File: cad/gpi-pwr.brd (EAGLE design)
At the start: 130 x 73.5 mm, 104 parts, among them CN1 HEADER-1X2, CN2 HEADER-3X1, CN3 HEADER-1X2.4, CN4 HEADER-3X12MM, Q1 MOSFETTO247REV, Q3 MOSFETTO247REV, Q5 MOSFETTO247REV, Q6 MOSFETTO247REV, Q7 MOSFETTO247REV, Q8 MOSFETTO247REV, U1 ACS709, U10 LM61, U11 MAX4452, U12 MAX4452, U2 ACS709, U3 ACPL-P346P346, U4 ACPL-P346P346, U5 ACPL-P346P346, U6 ACPL-P346P346, U7 ACPL-P346P346, U8 ACPL-P346P346, U9 LM61

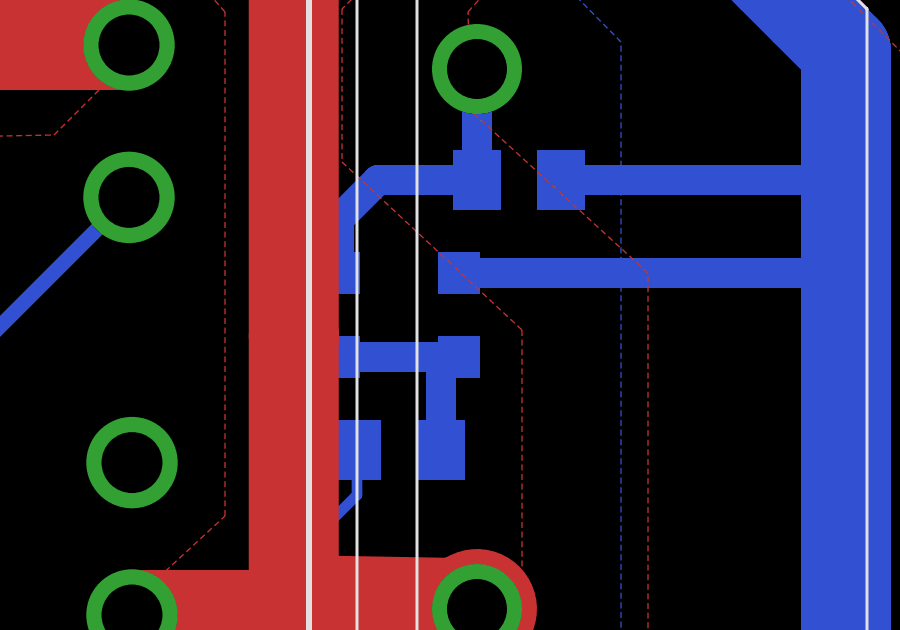
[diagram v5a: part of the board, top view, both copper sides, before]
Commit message: diode silk
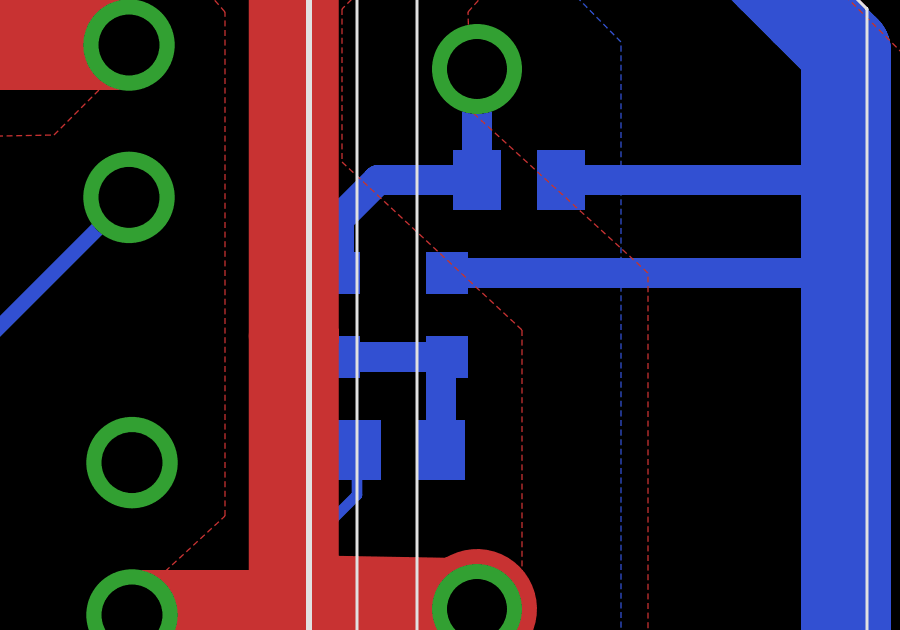
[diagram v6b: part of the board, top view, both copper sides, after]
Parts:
- moved D1 0.40 mm to (113.1, 50.0), turned to 270 degrees
- turned D2 to 270 degrees
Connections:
- net N$24: now also D1.A; no longer D1.C
- net N$25: now also D2.A; no longer D2.C
- net N$9: now also D1.C, D2.C; no longer D1.A, D2.A
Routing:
- net N$9: track 7.61 -> 6.82 mm

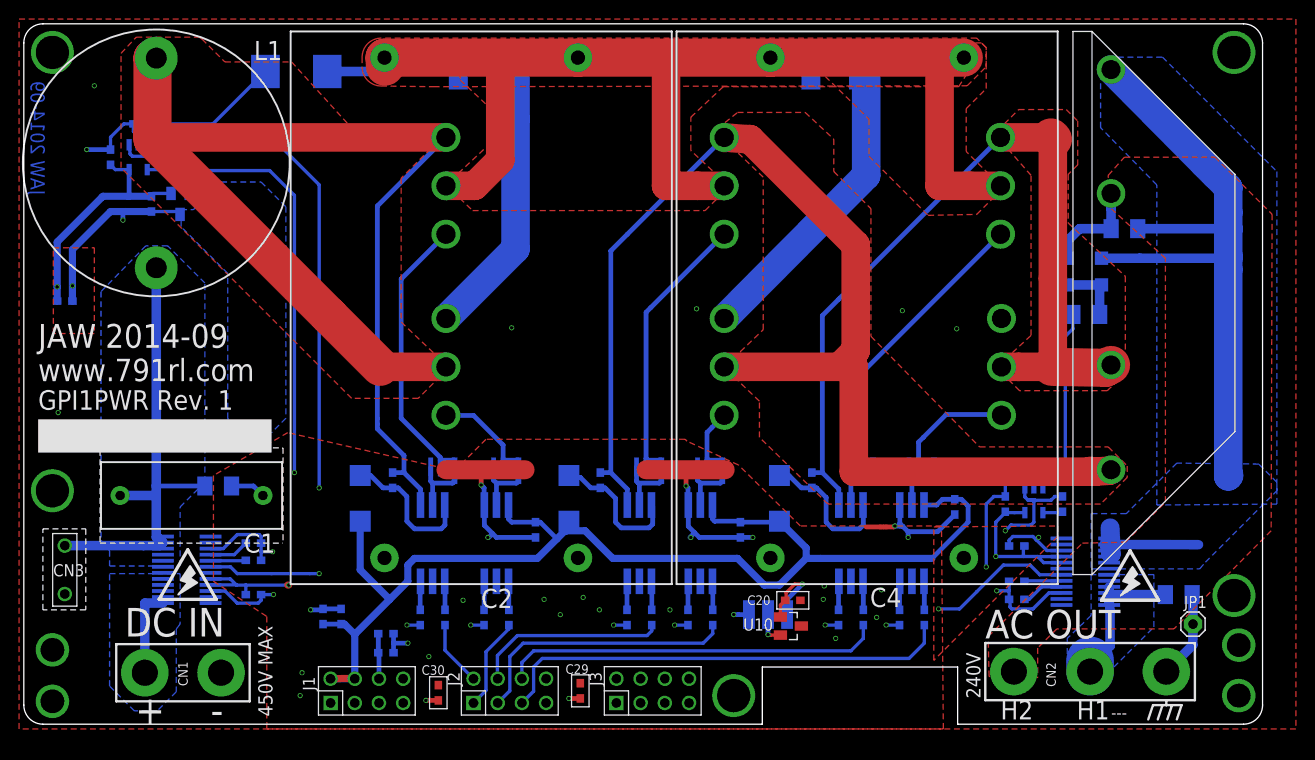
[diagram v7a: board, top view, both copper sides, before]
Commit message: revert opamp, tweak
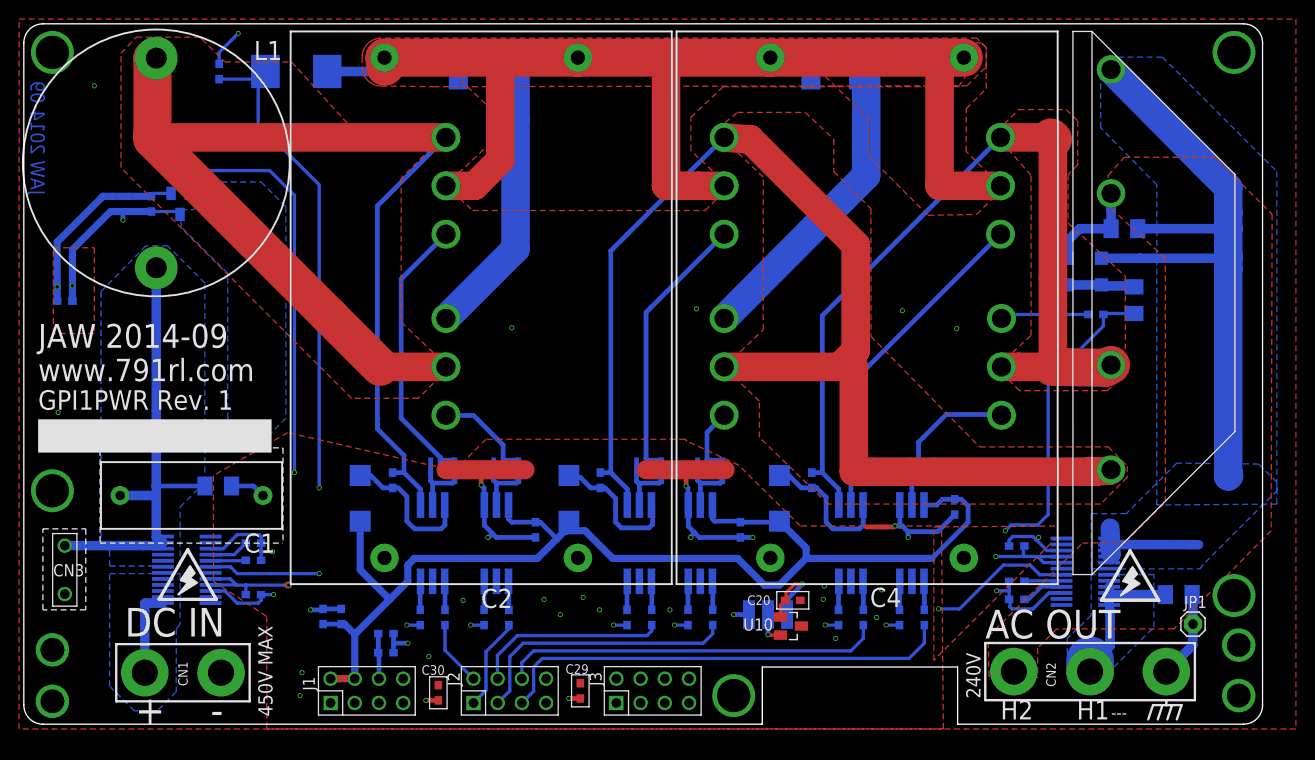
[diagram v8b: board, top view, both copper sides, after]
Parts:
- removed C27, C28: .1u, jaw:SMD0603
- removed R26, R27: 22, jaw:SMD0603
- removed U11, U12: MAX4452, jaw:SOT-23-5
- Q1, Q3, Q5, Q6, Q7, Q8: value MOSFETTO247REV -> C2M0160120D
- moved R10 17.1 mm to (112.5, 45.5)
- moved R5 9.87 mm to (20.5, 71.0), turned to 270 degrees
- moved R12 5.22 mm to (116.5, 47.0), turned to 270 degrees
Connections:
- removed net N$51: R26.1, U12.4
- removed net N$52: R27.1, U11.4
- removed net OP1: R1.P$1, R5.2, U11.3
- removed net OP2: R10.1, R12.2, U12.3
- net ADC2: now also R1.P$1, R5.2; no longer R27.2, U11.1
- net ADC3: now also R10.1, R12.2; no longer R26.2, U12.1
- net GND: now also R10.2
- net GNDM: no longer C27.2, C28.2, R10.2, U11.2, U12.2
- net VCC: no longer C27.1, C28.1, U11.5, U12.5
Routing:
- net GNDM: track 122.7 -> 101.6 mm, vias 31 -> 30
- net OP2: track 20.3 -> 0.00 mm
- net ADC3: track 60.5 -> 79.4 mm
- net OP1: track 16.8 -> 0.00 mm
- net GND: track 182.5 -> 194.3 mm
- net VCC: track 113.4 -> 101.7 mm
- net ADC2: track 94.0 -> 90.3 mm
- net N$52: track 2.26 -> 0.00 mm
- net N$51: track 2.07 -> 0.00 mm
- net N$9: track 6.82 -> 7.47 mm
